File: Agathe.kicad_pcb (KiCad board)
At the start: 2 copper layers, 338.8 x 114.8 mm, 170 parts, among them SW1 SW_Push, U1 ATmega32U4-AU, U2 PRTR5V0U2X, Y1 Crystal_GND24_Small

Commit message: WIP
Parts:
- added J1: Conn_01x04_Female, Connector_PinHeader_2.54mm:PinHeader_1x04_P2.54mm_Vertical, F.Cu at (167.7, 73.6)
- moved SW1 1.08 mm to (199.8, 78.7)
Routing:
- net D-: track 56.1 -> 85.2 mm
- net D+: track 61.4 -> 81.5 mm, vias 0 -> 2
- net VCC: track 20.6 -> 40.3 mm
- net LED: track 105.2 -> 108.5 mm
- net GND: track 256.8 -> 259.3 mm, vias 6 -> 7
- net Net-(R4-Pad2): track 72.2 -> 73.5 mm

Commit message: end
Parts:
- moved R5 5.97 mm to (183.8, 79.4), turned to 90 degrees
- moved F1 1.38 mm to (179.6, 81.5)
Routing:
- net Net-(R5-Pad2): track 7.09 -> 2.97 mm, vias 2 -> 0
- net +5V: track 978.1 -> 979.5 mm
- net GND: track 259.3 -> 260.7 mm, vias 7 -> 8
- net D+: track 81.5 -> 80.8 mm
- net VCC: track 40.3 -> 41.0 mm
- net D-: track 85.2 -> 85.7 mm

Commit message: end
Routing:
- net VCC: track 41.0 -> 40.0 mm

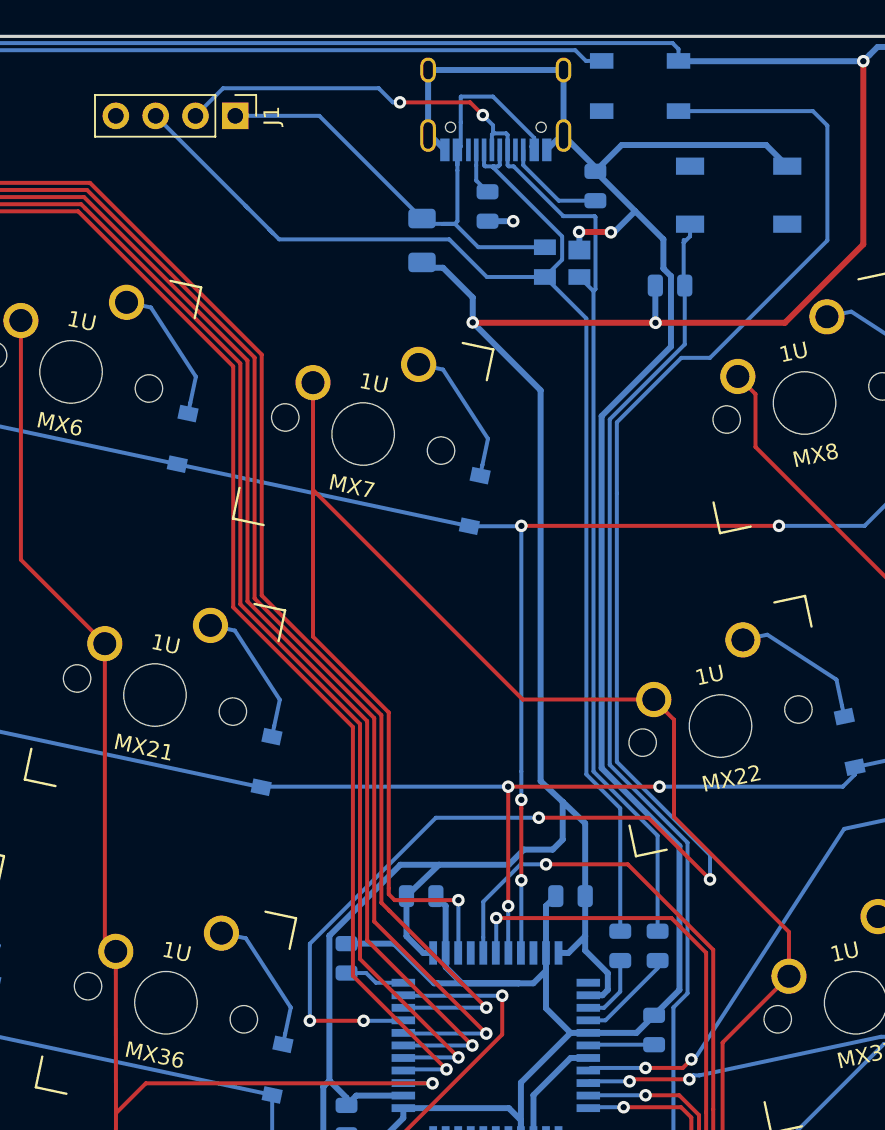
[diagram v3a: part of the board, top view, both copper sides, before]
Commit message: add 2 breakout header for VCC and GND
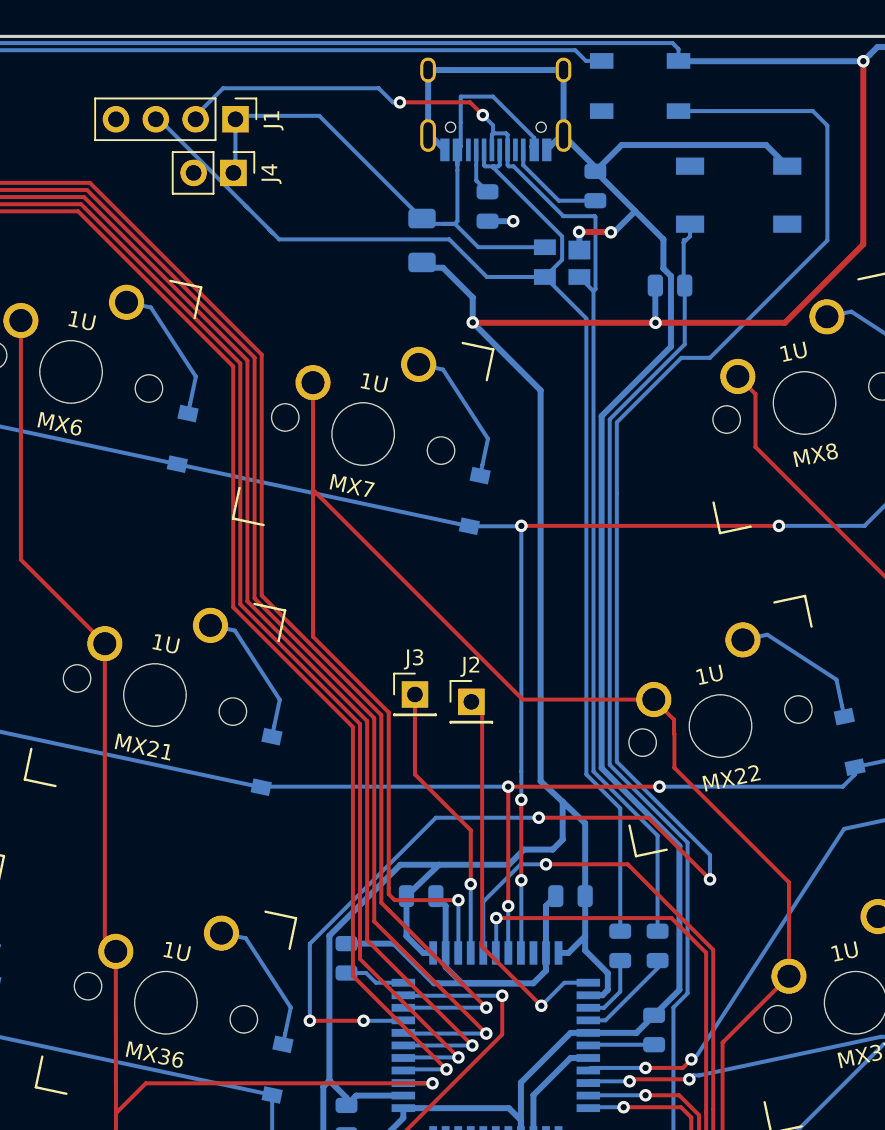
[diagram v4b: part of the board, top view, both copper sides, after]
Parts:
- added J2: GPIO 1, Connector_PinHeader_2.54mm:PinHeader_1x01_P2.54mm_Vertical, F.Cu at (182.8, 111.0)
- added J3: GPIO 2, Connector_PinHeader_2.54mm:PinHeader_1x01_P2.54mm_Vertical, F.Cu at (179.2, 110.5)
- added J4: Conn_01x02_Female, Connector_PinHeader_2.54mm:PinHeader_1x02_P2.54mm_Vertical, F.Cu at (167.6, 77.2)
- moved J1 0.22 mm to (167.7, 73.8)
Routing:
- net Net-(J2-Pad1): track 0.00 -> 24.8 mm, vias 0 -> 1
- net Net-(J3-Pad1): track 0.00 -> 18.0 mm, vias 0 -> 1
- net GND: track 260.7 -> 256.1 mm
- net VCC: track 40.0 -> 43.5 mm

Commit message: correct some routes
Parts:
- moved J4 0.50 mm to (167.6, 77.7)
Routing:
- net D-: track 85.7 -> 86.8 mm
- net D+: track 80.8 -> 80.3 mm

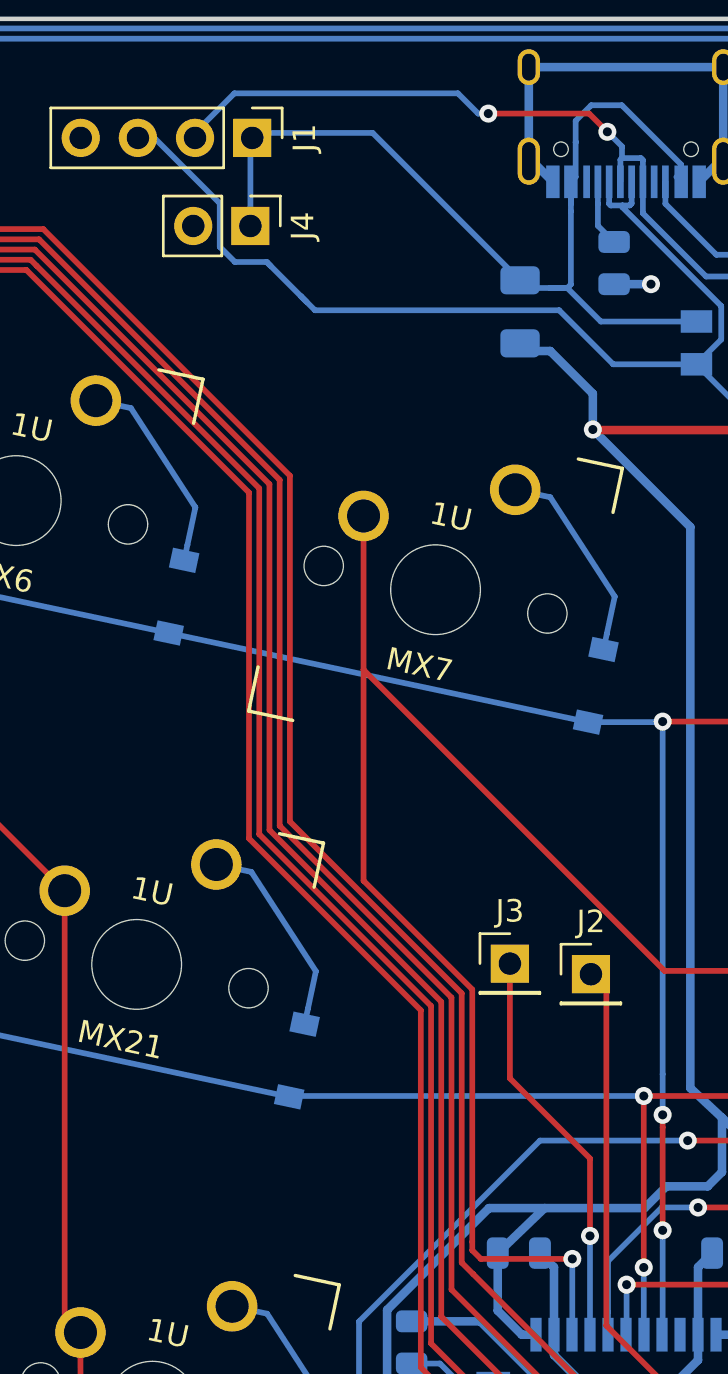
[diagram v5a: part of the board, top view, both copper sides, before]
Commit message: Realign J3 and J2. Reroute D- around J4
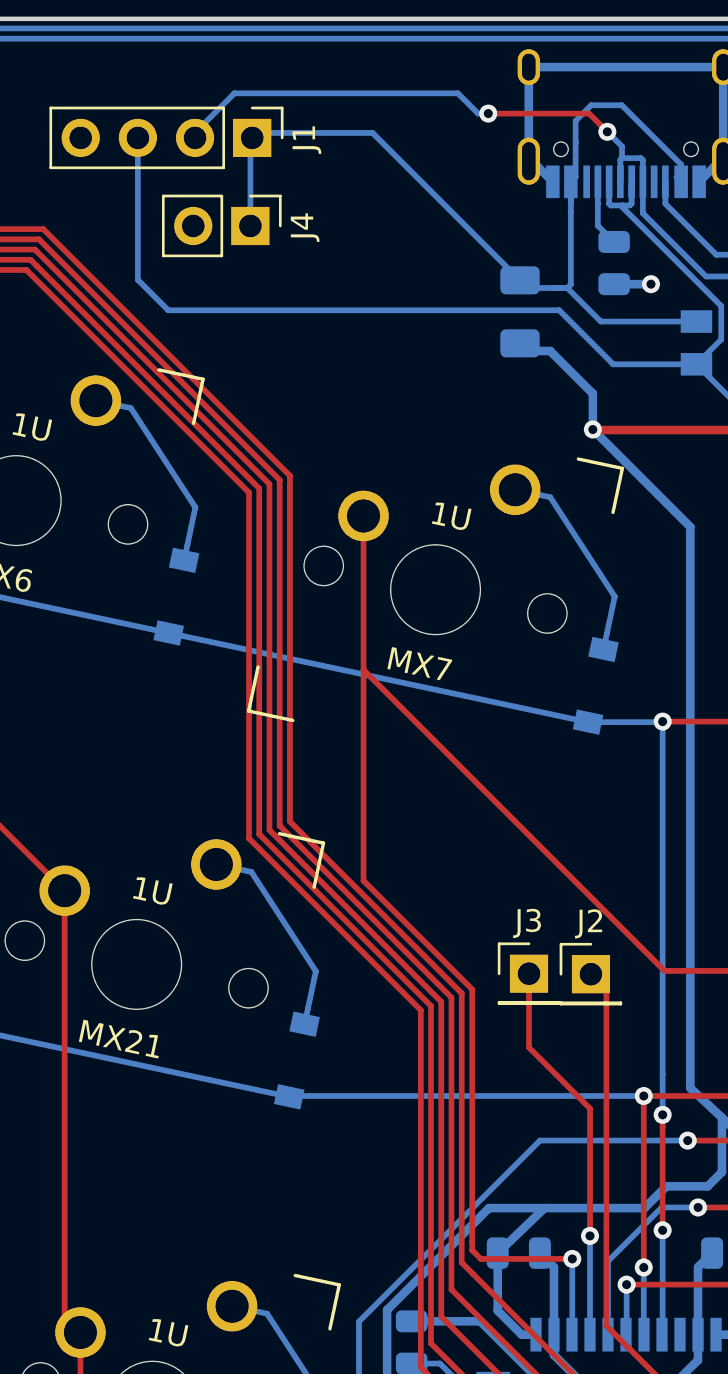
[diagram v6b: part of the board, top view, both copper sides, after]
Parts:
- moved J3 0.96 mm to (180.0, 111.0)
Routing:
- net D-: track 86.8 -> 89.5 mm
- net Net-(J3-Pad1): track 18.0 -> 17.2 mm

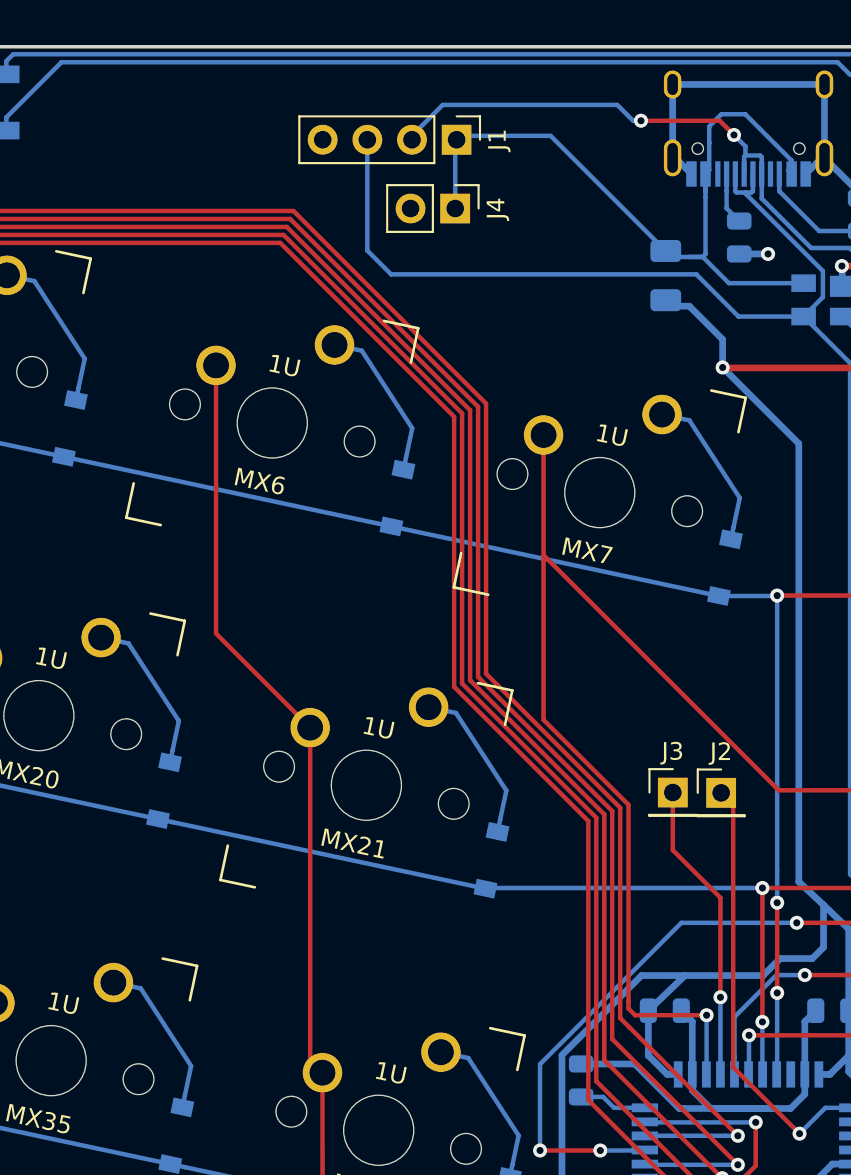
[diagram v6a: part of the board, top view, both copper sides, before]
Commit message: Move J2 to top
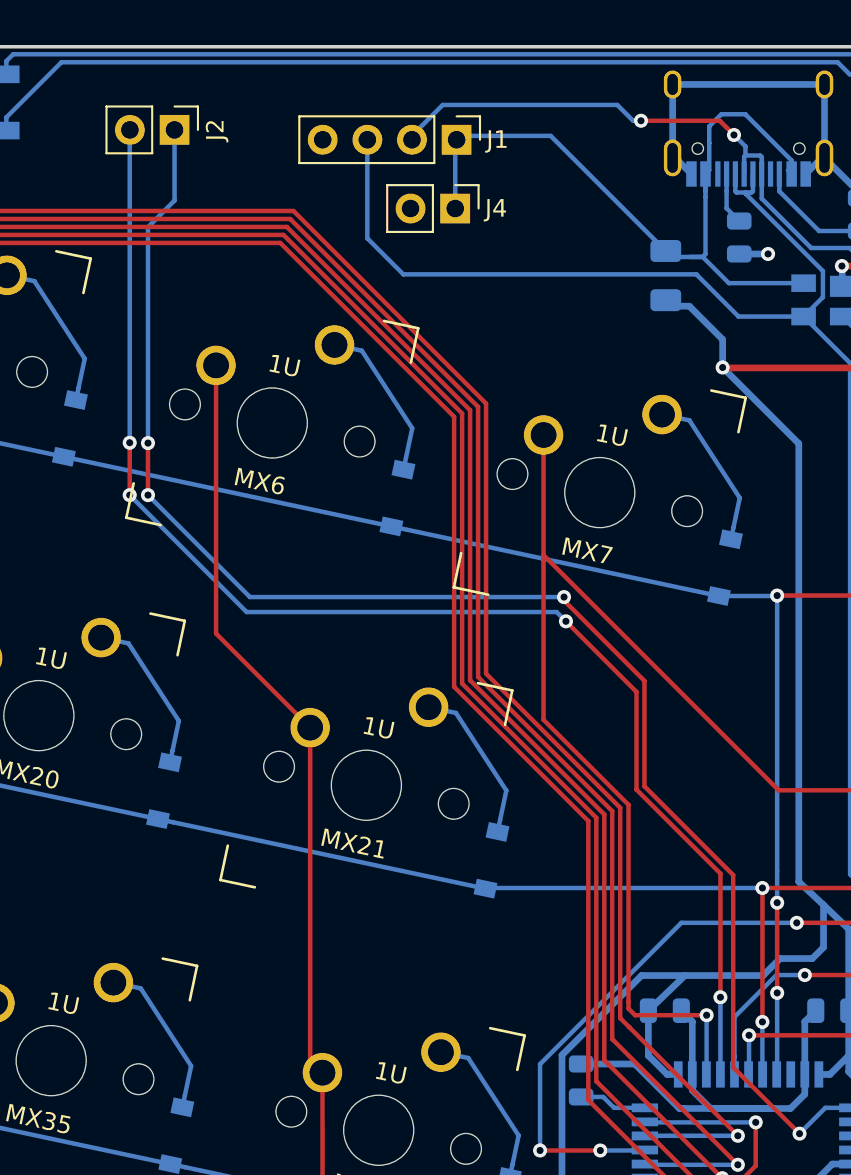
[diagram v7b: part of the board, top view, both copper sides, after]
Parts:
- removed J3: GPIO 2, Connector_PinHeader_2.54mm:PinHeader_1x01_P2.54mm_Vertical
- J2: value GPIO 1 -> Conn_01x02_Female; footprint Connector_PinHeader_2.54mm:PinHeader_1x01_P2.54mm_Vertical -> Connector_PinHeader_2.54mm:PinHeader_1x02_P2.54mm_Vertical
- R4: value R_Small -> 10k
- Y1: value Crystal_GND24_Small -> 16MHz
- moved J2 48.9 mm to (151.7, 73.2), turned to 270 degrees
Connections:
- net Net-(J2-Pad1) renamed GPIO1
- U1 pad 37: Net-(J3-Pad1) -> GPIO2
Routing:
- net GPIO2: track 0.00 -> 77.8 mm, vias 0 -> 4
- net GPIO1: track 24.8 -> 87.2 mm, vias 1 -> 4
- net Net-(J3-Pad1): track 17.2 -> 0.00 mm, vias 1 -> 0

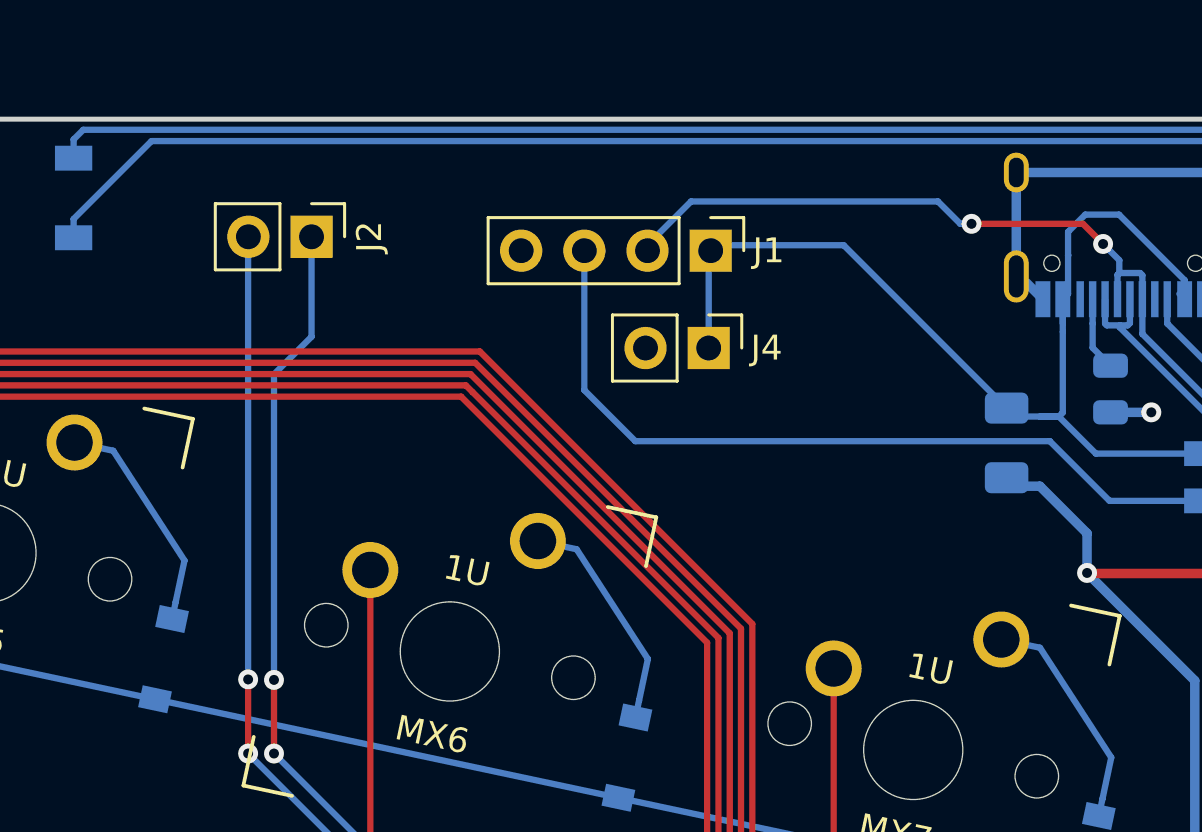
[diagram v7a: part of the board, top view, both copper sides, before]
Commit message: move breakout to the top
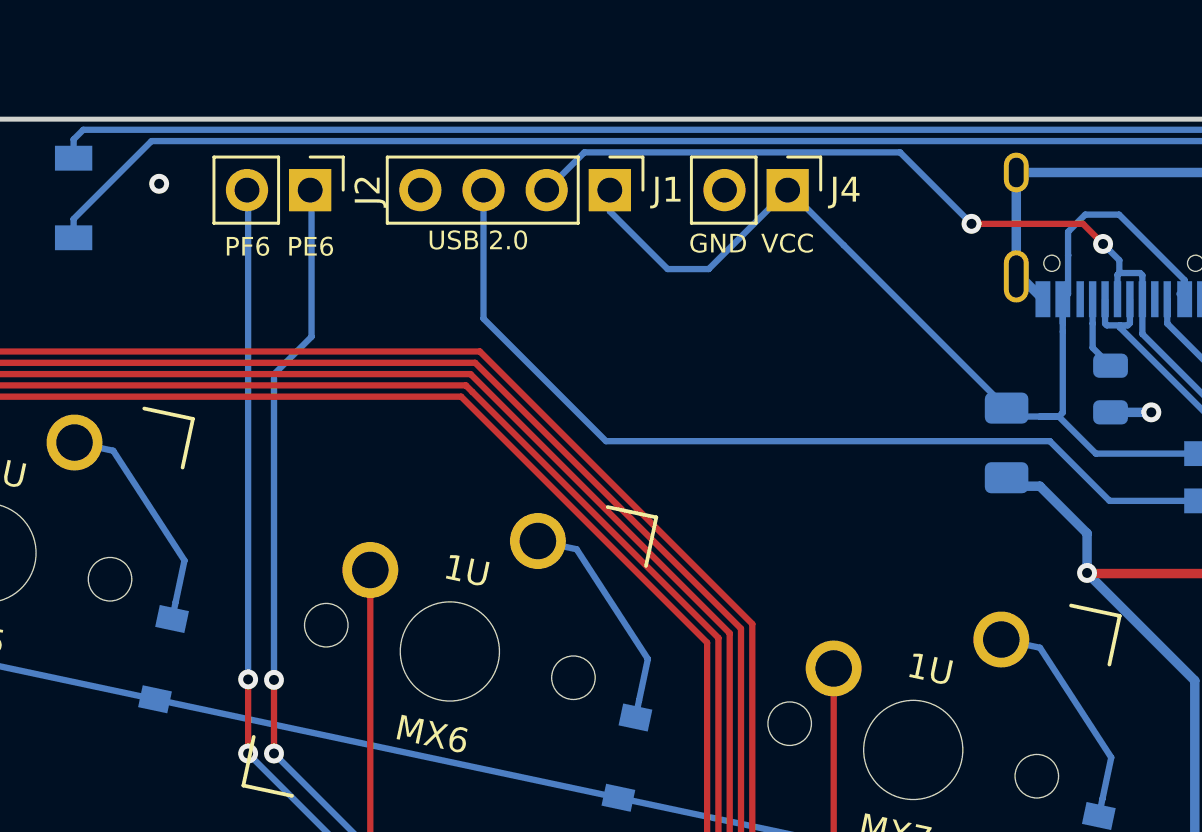
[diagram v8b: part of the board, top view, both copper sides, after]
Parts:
- moved J4 7.10 mm to (170.8, 71.4)
- moved J1 4.73 mm to (163.7, 71.4)
- moved J2 1.88 mm to (151.6, 71.4)
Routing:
- net D+: track 80.3 -> 85.0 mm
- net D-: track 89.1 -> 93.1 mm
- net VCC: track 43.7 -> 47.7 mm
- net GPIO2: track 77.8 -> 79.9 mm
- net GPIO1: track 87.2 -> 89.1 mm
- net GND: vias 8 -> 9
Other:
- board text added: "GND"
- board text added: "PE6"
- board text added: "PF6"
- board text added: "USB 2.0"
- board text added: "VCC"
